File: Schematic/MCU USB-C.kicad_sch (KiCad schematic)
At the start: 13 parts, among them Q18 BSS123, Q19 ZXMP10A13F, Q20 BSS123

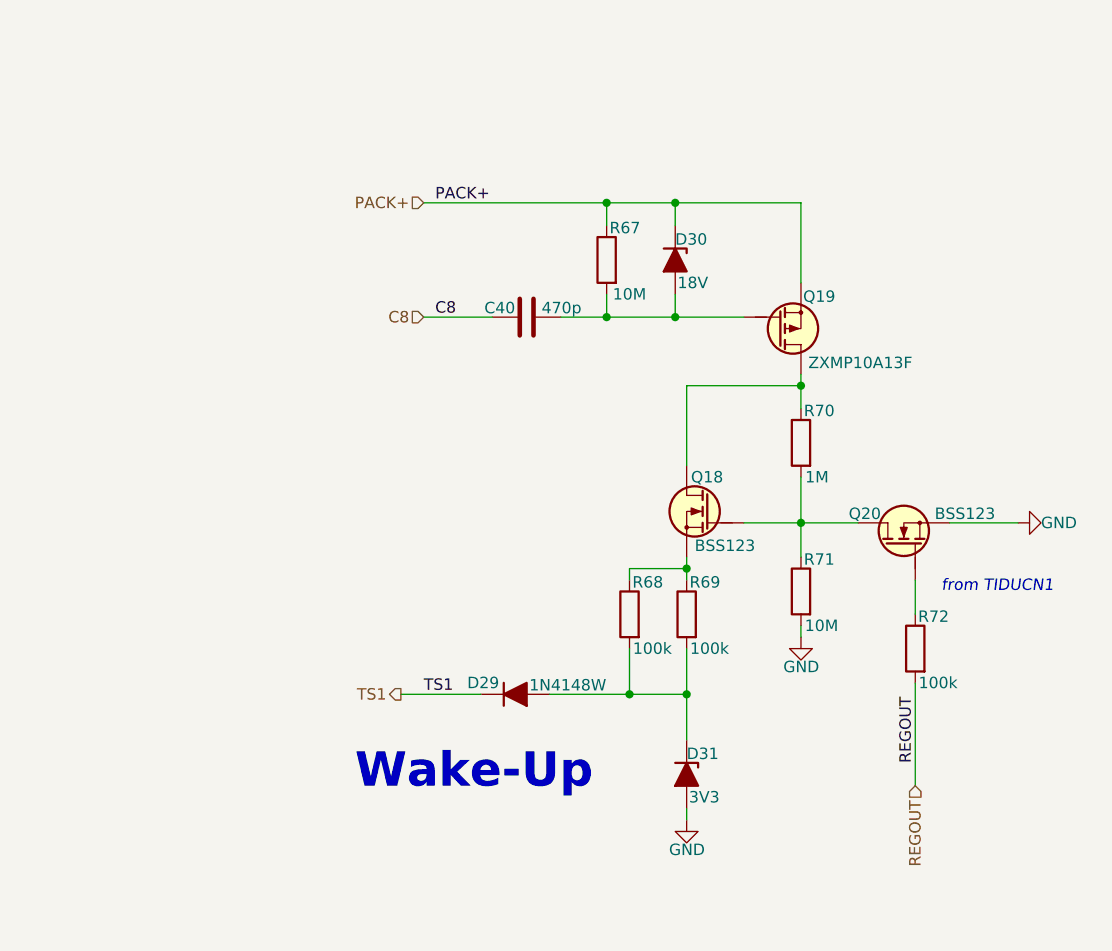
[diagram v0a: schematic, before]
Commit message: Added MCU
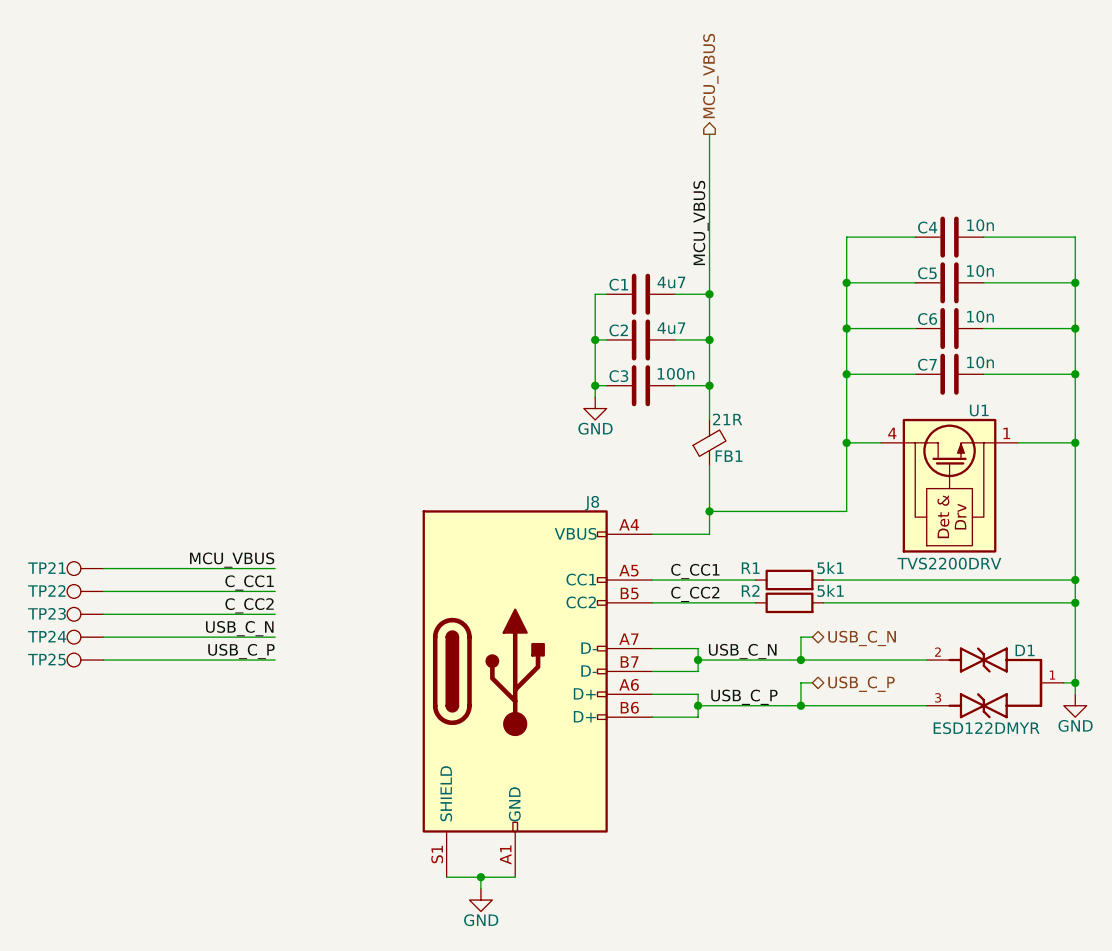
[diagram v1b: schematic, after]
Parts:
- removed C40: 470p, symbol Device:C
- removed D29: 1N4148W, PCM_Diode_SMD_AKL:D_SOD-123, symbol PCM_Diode_AKL:1N4148W
- removed D30: 18V, symbol Device:D_Zener_Filled
- removed D31: 3V3, symbol Device:D_Zener_Filled
- removed Q18, Q20: BSS123, PCM_Package_TO_SOT_SMD_AKL:SOT-23, symbol PCM_Transistor_MOSFET_AKL:BSS123
- removed Q19: ZXMP10A13F, PCM_Package_TO_SOT_SMD_AKL:SOT-23, symbol PCM_Transistor_MOSFET_AKL:ZXMP10A13F
- removed R67, R71: 10M, symbol Device:R
- removed R68, R69, R72: 100k, symbol Device:R
- removed R70: 1M, symbol Device:R
- added C1, C2: 4u7, symbol Device:C
- added C3: 100n, symbol Device:C
- added C4, C5, C6, C7: 10n, symbol Device:C
- added D1: ESD122DMYR, ESD122DMYR:DIO_ESD122DMYR, symbol ESD122:ESD122DMYR
- added FB1: 21R, symbol Device:FerriteBead_Small
- added J8: USB_C_Receptacle_USB2.0_14P, symbol Connector:USB_C_Receptacle_USB2.0_14P
- added R1, R2: 5k1, symbol Device:R
- added TP21, TP22, TP23, TP24, TP25: TestPoint, symbol Connector:TestPoint
- added U1: TVS2200DRV, Package_SON:WSON-6-1EP_2x2mm_P0.65mm_EP1x1.6mm, symbol Power_Protection:TVS2200DRV
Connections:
- net GND: now also C1.1, C2.1, C3.1, C4.2, C5.2, C6.2, C7.2, D1.1, J8.A1 (GND), J8.A12 (GND), J8.B1 (GND), J8.B12 (GND), J8.S1 (SHIELD), R1.2, R2.2, U1.1 (GND), U1.2 (GND), U1.3 (GND), U1.7 (GND)
- new net: C4.1, C5.1, C6.1, C7.1, FB1.1, J8.A4 (VBUS), J8.A9 (VBUS), J8.B4 (VBUS), J8.B9 (VBUS), U1.4 (IN), U1.5 (IN), U1.6 (IN)
- new net C_CC1: J8.A5 (CC1), R1.1, TP22.1
- new net C_CC2: J8.B5 (CC2), R2.1, TP23.1
- new net MCU_VBUS: C1.2, C2.2, C3.2, FB1.2, TP21.1
- new net USB_C_N: D1.2, J8.A7 (D-), J8.B7 (D-), TP24.1
- new net USB_C_P: D1.3, J8.A6 (D+), J8.B6 (D+), TP25.1
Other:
- note removed: "Wake-Up"
- note removed: "from TIDUCN1"

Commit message: Started to work on the BOM
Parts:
- C1, C2: footprint (none) -> Capacitor_SMD:C_1206_3216Metric_Pad1.33x1.80mm_HandSolder; Link (none) -> https://mou.sr/45jYGQI; Manufacturer Part Number (none) -> CL31B475KBHNFNE; Price per Unit (none) -> 0.27; Supplier (none) -> Mouser; Supplier Part Number (none) -> 187-CL31B475KBHNFNE
- C3: footprint (none) -> Capacitor_SMD:C_1206_3216Metric_Pad1.33x1.80mm_HandSolder; Link (none) -> https://mou.sr/4n9ybmQ; Manufacturer Part Number (none) -> CL31B104KBCNNNC; Price per Unit (none) -> 0.11; Supplier (none) -> Mouser; Supplier Part Number (none) -> 187-CL31B104KBCNNNC
- C4, C5, C6, C7: footprint (none) -> Capacitor_SMD:C_1206_3216Metric_Pad1.33x1.80mm_HandSolder; Link (none) -> https://mou.sr/3OC0xXF; Manufacturer Part Number (none) -> CL31B103KHFNFNE; Price per Unit (none) -> 0.13; Supplier (none) -> Mouser; Supplier Part Number (none) -> 187-CL31B103KHFNFNE
- D1: footprint ESD122DMYR:DIO_ESD122DMYR -> ESD122DMYR:ESD122DMYR; Link (none) -> https://mou.sr/46mVGTO; Manufacturer Part Number (none) -> ESD122DMYR; Price None -> (none); Price per Unit (none) -> 1.01; Supplier (none) -> Mouser; Supplier Part Number (none) -> 595-ESD122DMYR
- U1: footprint Package_SON:WSON-6-1EP_2x2mm_P0.65mm_EP1x1.6mm -> (none)

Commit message: Massive pivit, simplification
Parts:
- removed C1, C2: 4u7, Capacitor_SMD:C_1206_3216Metric_Pad1.33x1.80mm_HandSolder, symbol Device:C
- removed C3: 100n, Capacitor_SMD:C_1206_3216Metric_Pad1.33x1.80mm_HandSolder, symbol Device:C
- removed C4, C5, C6, C7: 10n, Capacitor_SMD:C_1206_3216Metric_Pad1.33x1.80mm_HandSolder, symbol Device:C
- removed D1: ESD122DMYR, ESD122DMYR:ESD122DMYR, symbol ESD122:ESD122DMYR
- removed FB1: 21R, symbol Device:FerriteBead_Small
- removed J8: USB_C_Receptacle_USB2.0_14P, symbol Connector:USB_C_Receptacle_USB2.0_14P
- removed R1, R2: 5k1, symbol Device:R
- removed TP21, TP22, TP23, TP24, TP25: TestPoint, symbol Connector:TestPoint
- removed U1: TVS2200DRV, symbol Power_Protection:TVS2200DRV
